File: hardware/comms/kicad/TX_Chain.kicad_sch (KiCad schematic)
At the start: 28 parts, among them Q1 2SC3356, U2 74LVC1G86, U6 ADL5602ARKZ-R7

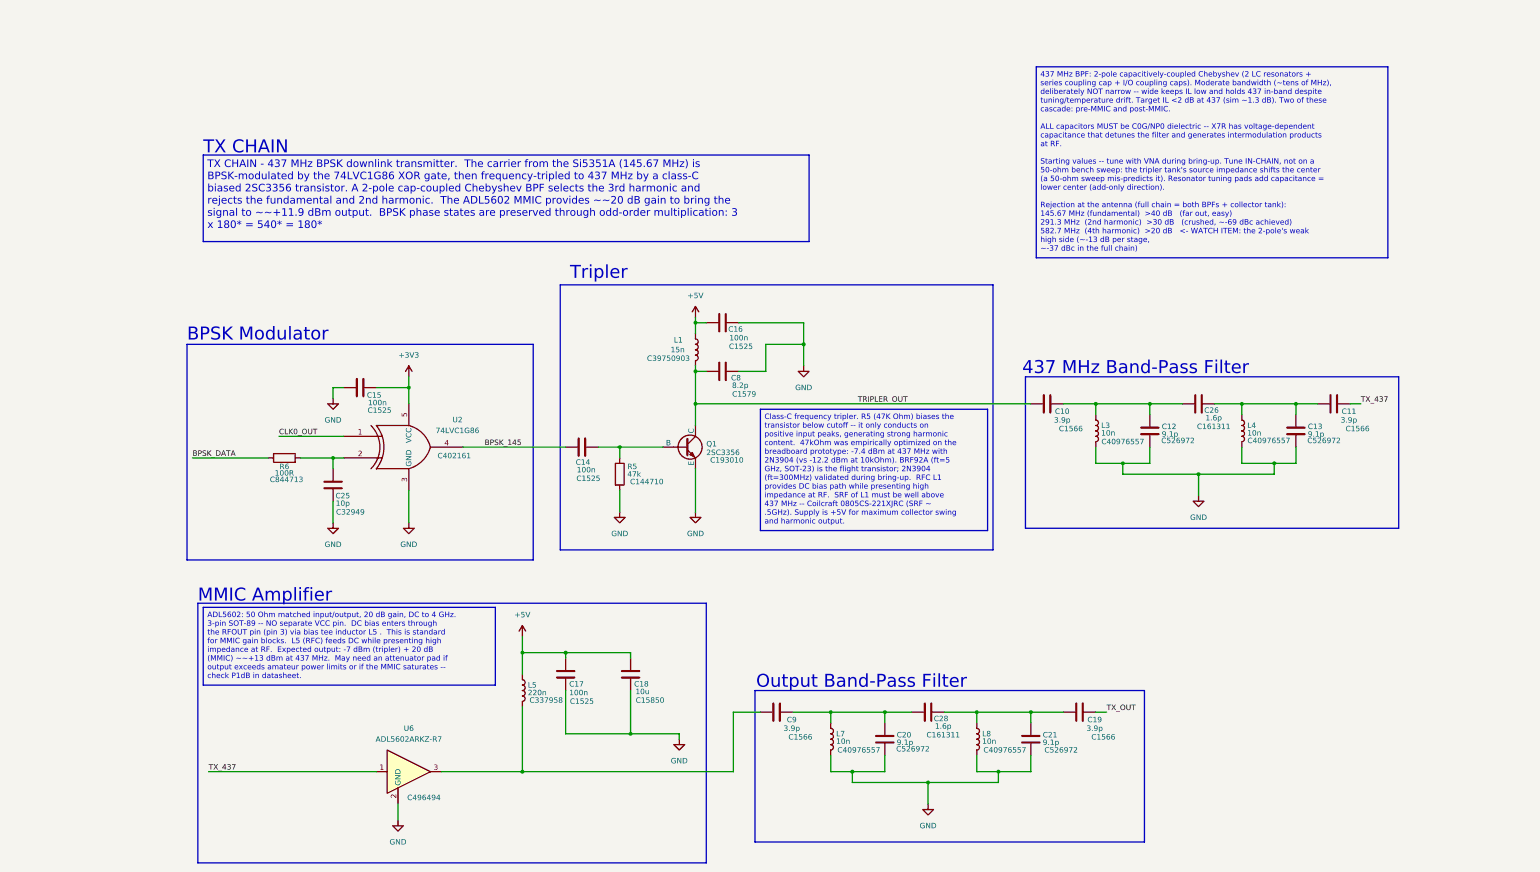
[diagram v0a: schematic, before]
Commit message: comms/kicad: rename project and sheets, correct schematic text
  Renames
  - transciever_kicad.{pro,sch,pcb} -> transceiver.{pro,sch,pcb}: the
    project name was misspelled, and the _kicad suffix was redundant
    inside a kicad/ directory.
  - Sheet files lose their spaces: Clock_Gen, Digital_Control, RX_Chain,
    TX_Chain. Sheetname keeps its space -- that is the label drawn on the
    sheet, not a path.
  - References updated in four places, not one: 4 Sheetfile properties in
    the root schematic, 186 per-symbol (project ...) instances across every
    sheet, 68 per-footprint (sheetfile ...) entries in the PCB, and
    meta.filename plus the root sheet name in the project file. Verified
    afterwards that all sheet references resolve, no sheet is orphaned, and
    the project file still parses.

  Spelling and stale labels
  - Title block: Revsion -> Revision, Repsoitory -> Repository, repository
    path centisat -> ember, project named EMBER.
  - PCI-104 -> CSKB in three files. PCI-104 is a different real standard,
    and the same sheet's own revision history records the bus being renamed
    to CSKB back at rev 0.4.
  - Status LED's -> Status LEDs; +20 db -> +20 dB; RX SMA < - -> <-.
  - The tripler note named BRF92A as the flight transistor: misspelled, and
    superseded by the 2SC3356 actually placed. Corrected to 2SC3356 with
    the MMBT3904-footprint note the implementation plan records. The
    ft=5 GHz figure is dropped rather than reassigned to a part it was not
    measured against.
  - Power sheet: the D4 forward-drop note referred to the SA612, replaced
    by the ADE-1+ back at rev 0.5. Now names the PSA4-5043+.
 Altium-to-KiCad text damage
  Three separate corruptions, classified before replacing so that real
  values were not caught up in it -- ~21 dB and ~20 dB both contain a
  literal ~2 and would have been mangled by a blind pass.
  - 144 table column separators rendered as literal ~2; now |, so the
    sheet index, rail summary, net c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
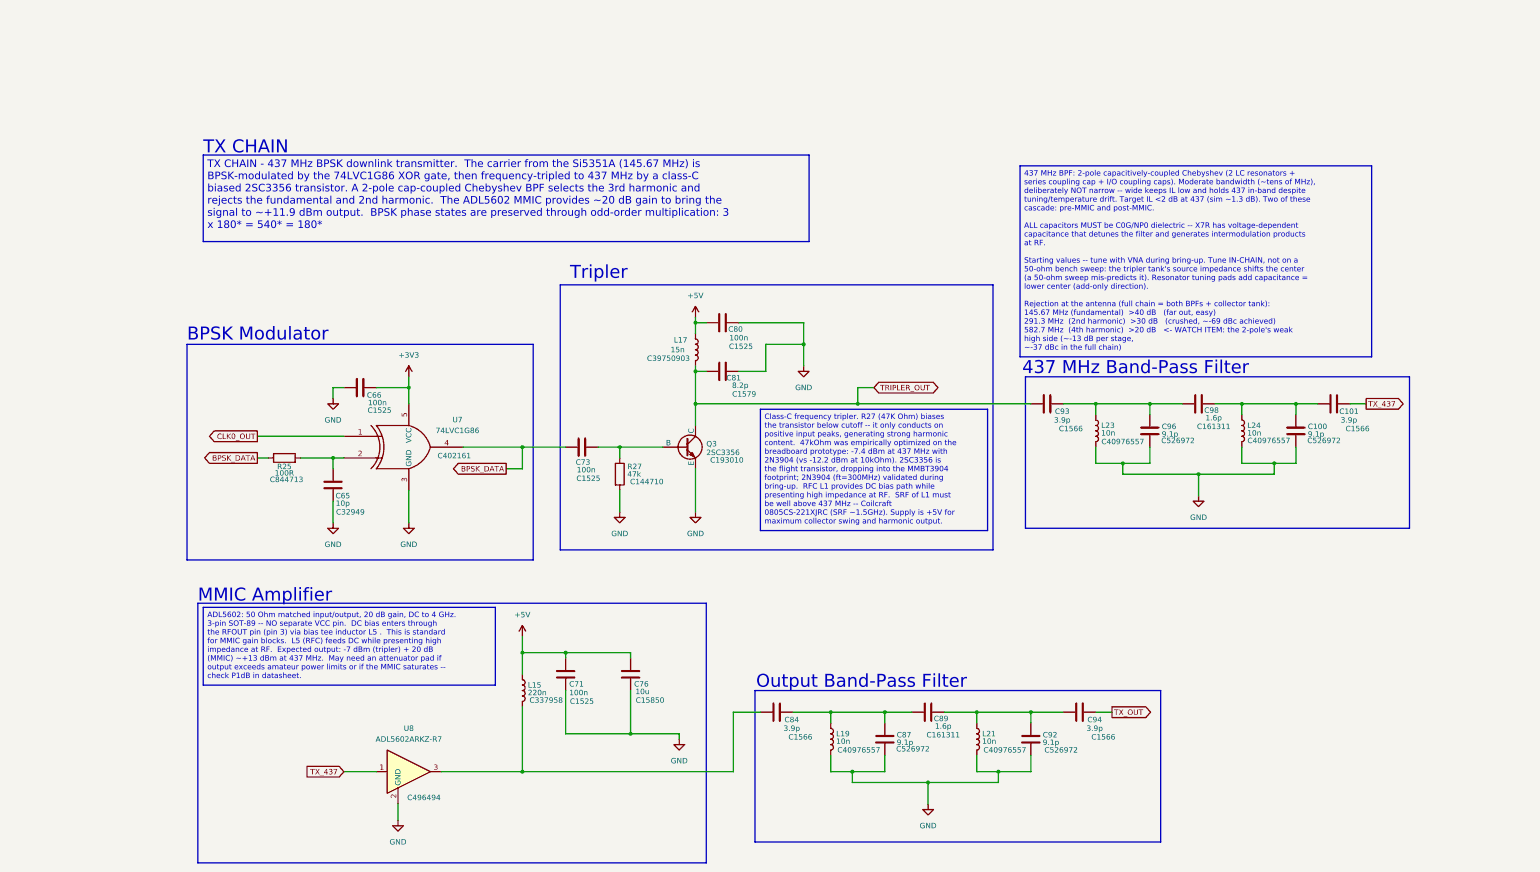
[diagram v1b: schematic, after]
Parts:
- renumbered C13 to C100, C11 to C101, C25 to C65, C15 to C66, C17 to C71, C14 to C73, C18 to C76, C16 to C80, C8 to C81, C9 to C84, C20 to C87, C28 to C89, C21 to C92, C10 to C93, C19 to C94, C12 to C96, C26 to C98, L5 to L15, L1 to L17, L7 to L19, L8 to L21, L3 to L23, L4 to L24, Q1 to Q3, R6 to R25, R5 to R27, U2 to U7, U6 to U8
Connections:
- net BPSK_145 is gone; now on net BPSK_DATA: C73.2, U7.4

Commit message: Repair UHF/UHF comms schematic and document PCB blockers
Correct PSA4 LNA and Hottech transistor pin mappings, RX capacitor values, and BPSK net labeling.

Assign verified XOR, resistor, and test-point footprints. Correct bulk capacitor polarity and add Panasonic land patterns.

Add project RF libraries, pin-map audit, and TOOD checklist. Record unresolved library loading, connectivity export, and PCB synchronization issues.
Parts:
- Q3: symbol Simulation_SPICE:NPN -> Transistor_BJT:Q_NPN_BEC; Manufacturer (none) -> Guangdong Hottech; Manufacturer Part # (none) -> 2SC3356
- U7: footprint (none) -> Package_TO_SOT_SMD:SOT-23-5; MPN (none) -> SN74LVC1G86DBVR; Manufacturer (none) -> Texas Instruments
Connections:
- net BPSK_DATA: no longer C73.2, U7.4
- net GND: now also Q3.2 (E); no longer Q3.3 (E)
- net TRIPLER_OUT: now also Q3.3 (C); no longer Q3.1 (C)
- net at C73.1, R27.1: now also Q3.1 (B); no longer Q3.2 (B)
- new net RF_TX_BPSK_145: C73.2, U7.4
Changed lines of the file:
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@@
 		(rev "B")
 		(comment 1 "Nick Grabbs - KI5YNG")
+		(comment 9 "UHF/UHF revision in review - not for fabrication")
 	)
 	(rectangle
@@
 		)
 	)
-	(global_label "CLK0_OUT"
-		(shape output)
-		(at 87.63 121.92 180)
-		(fields_autoplaced yes)
+	(label "RF_TX_BPSK_145"
+		(at 146.05 129.54 180)
 		(effects
 			(font
 				(size 1.27 1.27)
 			)
-			(justify right)
-		)
-		(property "Intersheetrefs" "${INTERSHEET_REFS}"
-			(at 75.271 121.92 0)
-			(hide yes)
-			(show_name no)
-			(do_not_autoplace no)
-			(effects
-				(font
-					(size 1.27 1.27)
-				)
-				(justify right)
-			)
+			(justify right bottom)
 		)
 	)
-	(global_label "BPSK_DATA"
+	(global_label "CLK0_OUT"
 		(shape output)
-		(at 146.05 129.54 180)
-		(fields_autoplaced yes)
+		(at 87.63 121.92 180)
 		(effects
 			(font
@@
 		)
 		(property "Intersheetrefs" "${INTERSHEET_REFS}"
-			(at 132.6629 129.54 0)
+			(at 75.271 121.92 0)
 			(hide yes)
 			(show_name no)
@@
 		(shape output)
 		(at 288.29 186.69 0)
-		(fields_autoplaced yes)
 		(effects
 			(font
@@
 		(shape output)
 		(at 87.63 127 180)
-		(fields_autoplaced yes)
 		(effects
 			(font
@@
 		(shape bidirectional)
 		(at 232.41 110.49 0)
-		(fields_autoplaced yes)
 		(effects
 			(font
@@
 		(shape input)
 		(at 107.95 200.66 180)
-		(fields_autoplaced yes)
 		(effects
 			(font
@@
 		(shape output)
 		(at 347.98 114.3 0)
-		(fields_autoplaced yes)
 		(effects
 			(font
@@
 	)
 	(symbol
-		(lib_id "Simulation_SPICE:NPN")
+		(lib_id "Transistor_BJT:Q_NPN_BEC")
 		(at 187.96 124.46 0)
 		(unit 1)
@@
 			)
 		)
-		(property "Datasheet" "https://ngspice.sourceforge.io/docs/ngspice-html-manual/manual.xhtml#cha_BJTs"
+		(property "Datasheet" "https://www.lcsc.com/datasheet/C193010.pdf"
 			(at 251.46 124.46 0)
 			(hide yes)
@@
 			)
 		)
-		(property "Description" "Bipolar transistor symbol for simulation only, substrate tied to the emitter"
+		(property "Description" "Hottech 2SC3356 SOT-23; B=1 E=2 C=3; do not substitute Renesas pinout"
 			(at 187.96 124.46 0)
 			(hide yes)
@@
 			)
 		)
-		(property "Sim.Pins" "1=C 2=B 3=E"
+		(property "Sim.Pins" "1=B 2=E 3=C"
 			(at 187.96 124.46 0)
 			(hide yes)
@@
 			)
 		)
+		(property "Manufacturer" "Guangdong Hottech"
+			(at 187.96 124.46 0)
+			(hide yes)
+			(show_name no)
+			(do_not_autoplace no)
+			(effects
+				(font
+					(size 1.27 1.27)
+				)
+			)
+		)
+		(property "Manufacturer Part #" "2SC3356"
+			(at 187.96 124.46 0)
+			(hide yes)
+			(show_name no)
+			(do_not_autoplace no)
+			(effects
+				(font
+					(size 1.27 1.27)
+				)
+			)
+		)
 		(pin "2"
 		)
@@
 			)
 		)
-		(property "Footprint" ""
+		(property "Footprint" "Package_TO_SOT_SMD:SOT-23-5"
 			(at 123.19 124.46 0)
 			(hide yes)
@@
 			)
 		)
-		(property "Datasheet" "http://www.ti.com/lit/sg/scyt129e/scyt129e.pdf"
+		(property "Datasheet" "https://www.ti.com/lit/ds/symlink/sn74lvc1g86.pdf"
 			(at 123.19 124.46 0)
 			(hide yes)
@@
 			)
 		)
-	)
+		(property "MPN" "SN74LVC1G86DBVR"
+			(at 123.19 124.46 0)
+			(hide yes)
+			(effects
+				(font
+					(size 1.27 1.27)
+				)
+			)
+		)
+		(property "Manufacturer" "Texas Instruments"
+			(at 123.19 124.46 0)
+			(hide yes)
+			(effects
+				(font
+					(size 1.27 1.27)
+				)
+			)
+		))
 	(symbol
 		(lib_id "power:GND")

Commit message: Checkpoint validated single-antenna comms routing before placement optimization
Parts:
- U8: MPN (none) -> ADL5602ARKZ-R7; Manufacturer (none) -> Analog Devices; PinMapAudit (none) -> design/u8_adl5602_pinmap.md
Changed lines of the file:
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@@
 			)
 		)
-		(property "Datasheet" "https://www.analog.com/media/en/technical-documentation/data-sheets/ADL5610.pdf"
+		(property "Datasheet" "https://www.analog.com/media/en/technical-documentation/data-sheets/ADL5602.pdf"
 			(at 123.19 200.66 0)
 			(hide yes)
@@
 			)
 		)
-		(property "Description" "30-6000MHz RF/IF +18.4dB gain block, SOT-89"
+		(property "Description" "ADL5602 50 MHz to 4 GHz RF/IF gain block, 20 dB nominal, 5 V, SOT-89; audited pin-compatible ADL5610 symbol"
 			(at 123.19 200.66 0)
 			(hide yes)
@@
 			(show_name no)
 			(do_not_autoplace no)
+			(effects
+				(font
+					(size 1.27 1.27)
+				)
+			)
+		)
+		(property "MPN" "ADL5602ARKZ-R7"
+			(at 123.19 200.66 0)
+			(hide yes)
+			(show_name no)
+			(do_not_autoplace no)
+			(effects
+				(font
+					(size 1.27 1.27)
+				)
+			)
+		)
+		(property "Manufacturer" "Analog Devices"
+			(at 123.19 200.66 0)
+			(hide yes)
+			(show_name no)
+			(do_not_autoplace no)
+			(effects
+				(font
+					(size 1.27 1.27)
+				)
+			)
+		)
+		(property "PinMapAudit" "design/u8_adl5602_pinmap.md"
+			(at 123.19 200.66 0)
+			(hide yes)
+			(show_name no)
+			(do_not_autoplace no)

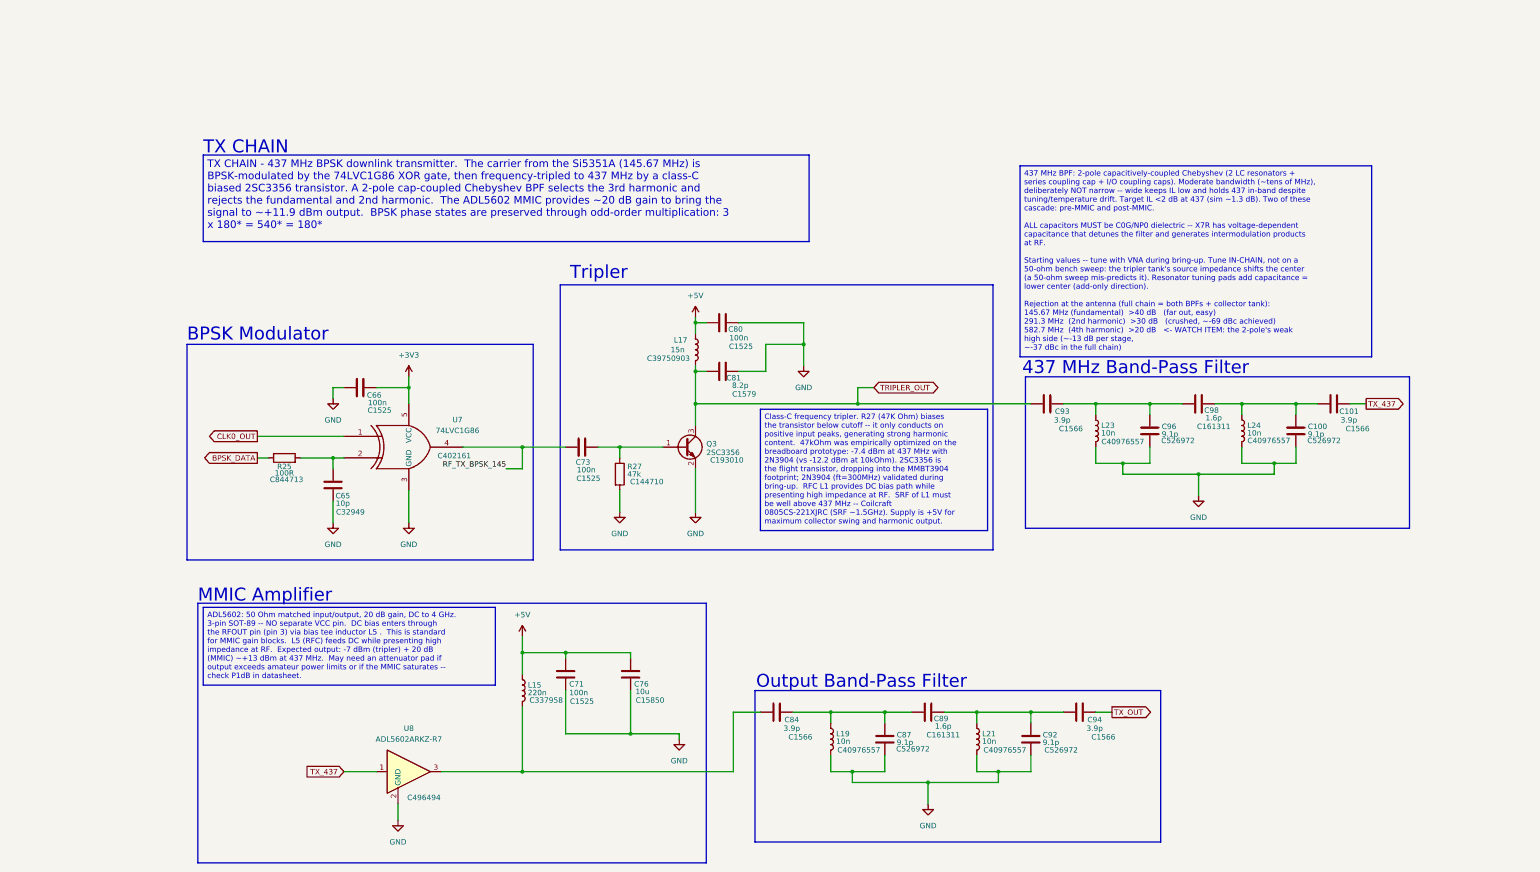
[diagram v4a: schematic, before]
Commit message: Complete dual-CAN transceiver hardware prototype
Preserve the current transceiver schematics, PCB, libraries and validation evidence as a focused hardware review against main.
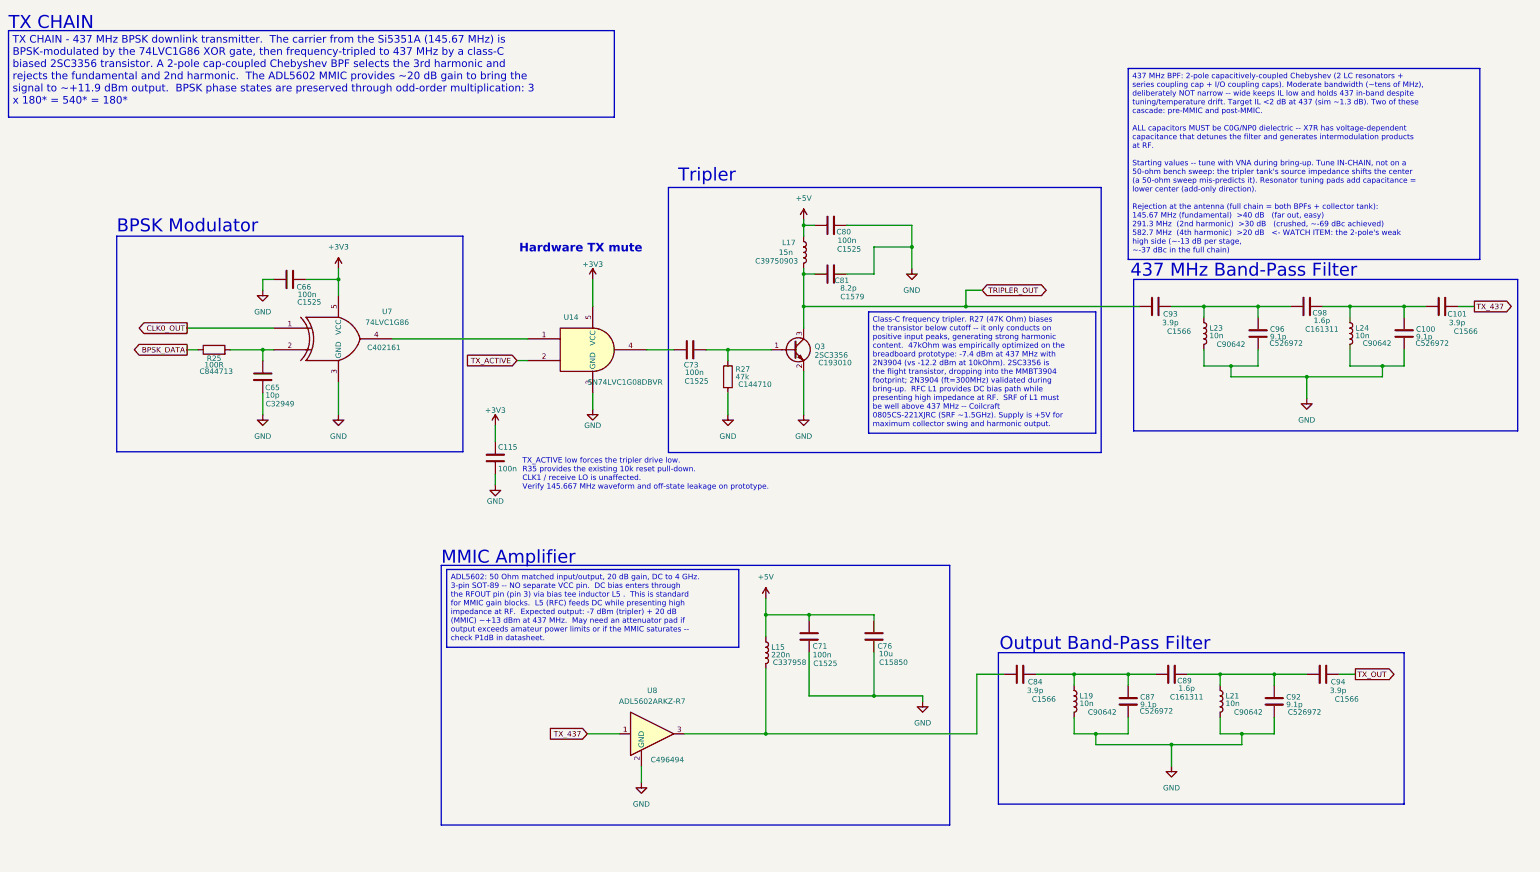
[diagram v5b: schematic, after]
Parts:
- added C115: 100n, Capacitor_SMD:C_0402_1005Metric, symbol Device:C
- added U14: SN74LVC1G08DBVR, Package_TO_SOT_SMD:SOT-23-5, symbol 74xGxx:74LVC1G08
- L19, L21, L23, L24: LCSC Part # C40976557 -> C90642; MPN (none) -> LQW15AN10NG00D; Manufacturer (none) -> Murata Electronics
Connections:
- net +3V3: now also C115.1, U14.5 (VCC)
- net GND: now also C115.2, U14.3 (GND)
- net RF_TX_BPSK_145: no longer names the net of C73.2
- net RF_TX_BPSK_145: now also U14.4; no longer U7.4
- new net: U14.1, U7.4
- new net TX_ACTIVE: U14.2
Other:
- note added: "Hardware TX mute"
- note added: "TX_ACTIVE low forces the tripler drive low. R35 provides the existing 10k reset pull-down. CLK1 / receive LO is unaffected. Verify 145.667 MHz waveform and off-state leakage on prototype."
- moved on the sheet: C100, C101, C65, C66, C71, C73, C76, C80, C81, C84, C87, C89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
